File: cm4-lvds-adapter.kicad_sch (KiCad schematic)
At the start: 19 parts, among them J1 Plug_Molex_SlimStack_2x15_538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, J2 JST_SM_1x10_SM10B-SURS-TF-LF-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

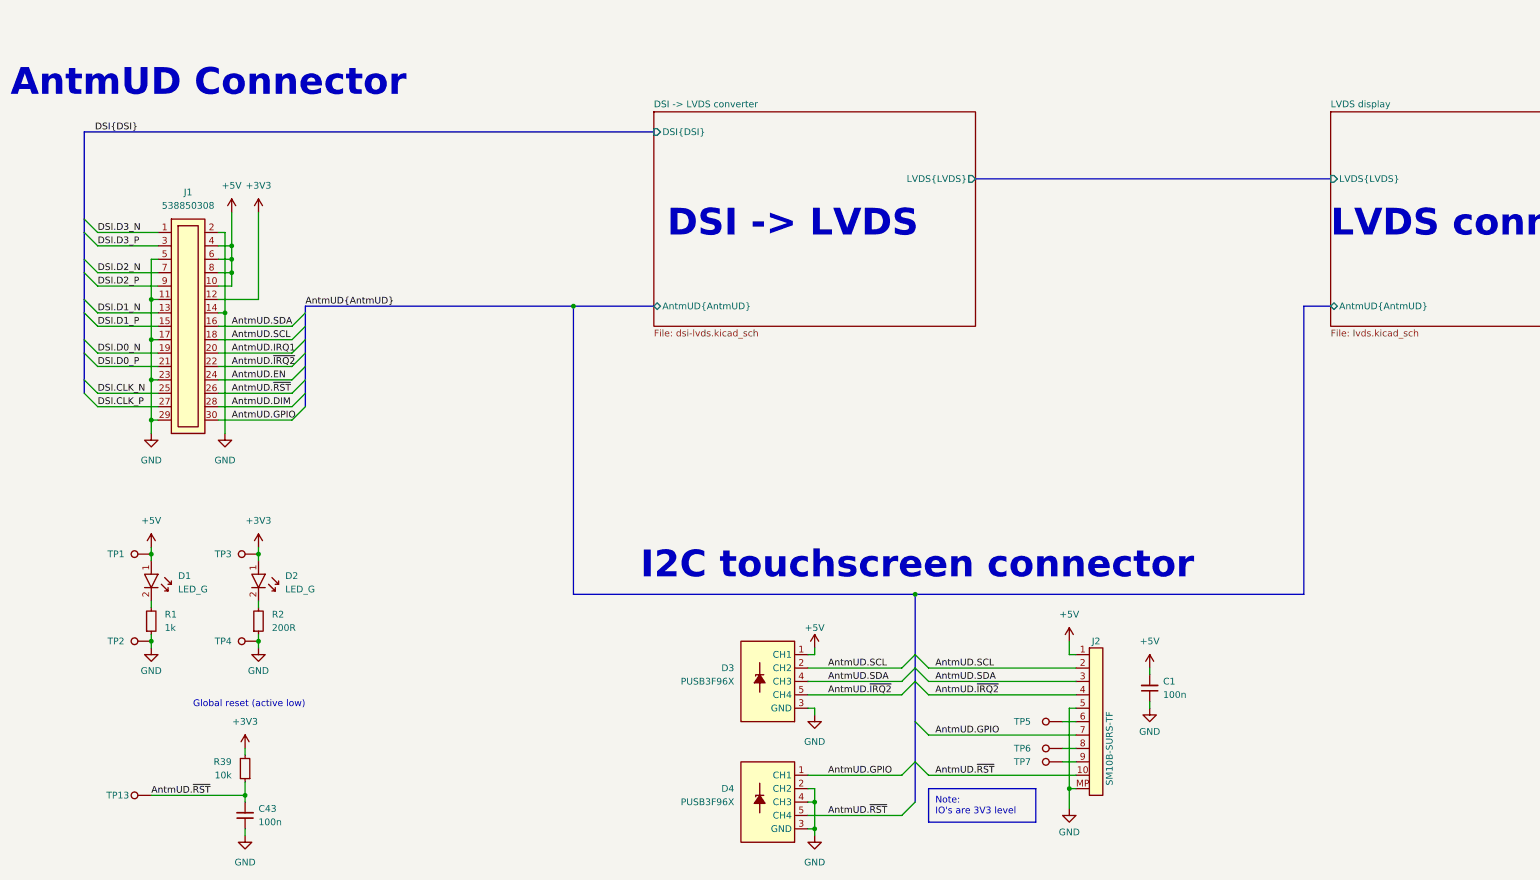
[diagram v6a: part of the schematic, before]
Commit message: [#54932] Sch: update net labels
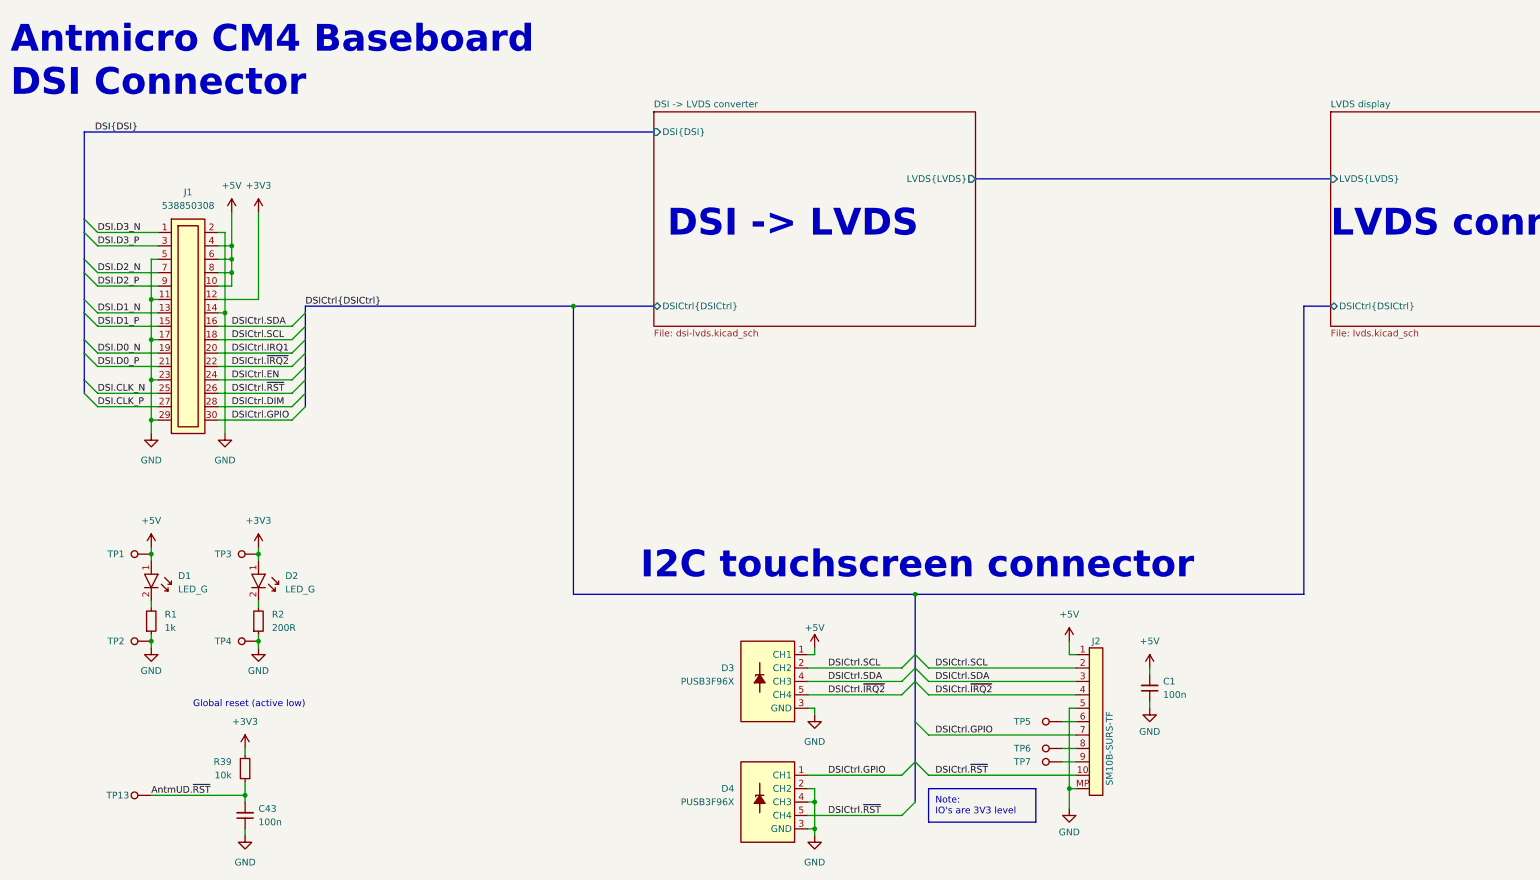
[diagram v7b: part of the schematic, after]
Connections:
- net AntmUD.~{RST}: no longer D4.5 (CH4), D4.6 (CH4), J1.26, J2.10
- net AntmUD.DIM renamed DSICtrl.DIM
- net AntmUD.EN renamed DSICtrl.EN
- net AntmUD.GPIO renamed DSICtrl.GPIO
- net AntmUD.IRQ1 renamed DSICtrl.IRQ1
- net AntmUD.SCL renamed DSICtrl.SCL
- net AntmUD.SDA renamed DSICtrl.SDA
- net AntmUD.~{IRQ2} renamed DSICtrl.~{IRQ2}
- new net DSICtrl.~{RST}: D4.5 (CH4), D4.6 (CH4), J1.26, J2.10
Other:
- sheet DSI -> LVDS converter ports: added DSICtrl{DSICtrl}; removed AntmUD{AntmUD}
- sheet LVDS display ports: added DSICtrl{DSICtrl}; removed AntmUD{AntmUD}
- note added: "Antmicro CM4 Baseboard DSI Connector"
- note removed: "AntmUD Connector"
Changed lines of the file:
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@@
     (effects (font (size 1.27 1.27)) (justify right bottom))
   )
-  (text "AntmUD Connector" (at 60.96 85.09 0)
+  (text "Antmicro CM4 Baseboard \nDSI Connector" (at 60.96 85.09 0)
     (effects (font (size 5.08 5.08) (thickness 1.016) bold) (justify left bottom))
   )
@@
     (effects (font (size 1.27 1.27)) (justify left bottom))
   )
-  (label "AntmUD.~{IRQ2}" (at 215.9 198.12 0) (fields_autoplaced)
-    (effects (font (size 1.27 1.27)) (justify left bottom))
-  )
-  (label "AntmUD.SCL" (at 215.9 193.04 0) (fields_autoplaced)
-    (effects (font (size 1.27 1.27)) (justify left bottom))
-  )
-  (label "AntmUD.SDA" (at 102.87 128.27 0) (fields_autoplaced)
-    (effects (font (size 1.27 1.27)) (justify left bottom))
-  )
-  (label "AntmUD.SDA" (at 215.9 195.58 0) (fields_autoplaced)
+  (label "DSICtrl.~{IRQ2}" (at 215.9 198.12 0) (fields_autoplaced)
+    (effects (font (size 1.27 1.27)) (justify left bottom))
+  )
+  (label "DSICtrl.SCL" (at 215.9 193.04 0) (fields_autoplaced)
+    (effects (font (size 1.27 1.27)) (justify left bottom))
+  )
+  (label "DSICtrl.SDA" (at 102.87 128.27 0) (fields_autoplaced)
+    (effects (font (size 1.27 1.27)) (justify left bottom))
+  )
+  (label "DSICtrl.SDA" (at 215.9 195.58 0) (fields_autoplaced)
     (effects (font (size 1.27 1.27)) (justify left bottom))
   )
@@
     (effects (font (size 1.27 1.27)) (justify right bottom))
   )
-  (label "AntmUD.SCL" (at 236.22 193.04 0) (fields_autoplaced)
-    (effects (font (size 1.27 1.27)) (justify left bottom))
-  )
-  (label "AntmUD.~{RST}" (at 215.9 220.98 0) (fields_autoplaced)
-    (effects (font (size 1.27 1.27)) (justify left bottom))
-  )
-  (label "AntmUD.SDA" (at 236.22 195.58 0) (fields_autoplaced)
-    (effects (font (size 1.27 1.27)) (justify left bottom))
-  )
-  (label "AntmUD.EN" (at 102.87 138.43 0) (fields_autoplaced)
-    (effects (font (size 1.27 1.27)) (justify left bottom))
-  )
-  (label "AntmUD{AntmUD}" (at 116.84 124.46 0) (fields_autoplaced)
-    (effects (font (size 1.27 1.27)) (justify left bottom))
-  )
-  (label "AntmUD.~{IRQ2}" (at 102.87 135.89 0) (fields_autoplaced)
-    (effects (font (size 1.27 1.27)) (justify left bottom))
-  )
-  (label "AntmUD.SCL" (at 102.87 130.81 0) (fields_autoplaced)
+  (label "DSICtrl.SCL" (at 236.22 193.04 0) (fields_autoplaced)
+    (effects (font (size 1.27 1.27)) (justify left bottom))
+  )
+  (label "DSICtrl.~{RST}" (at 215.9 220.98 0) (fields_autoplaced)
+    (effects (font (size 1.27 1.27)) (justify left bottom))
+  )
+  (label "DSICtrl.SDA" (at 236.22 195.58 0) (fields_autoplaced)
+    (effects (font (size 1.27 1.27)) (justify left bottom))
+  )
+  (label "DSICtrl.EN" (at 102.87 138.43 0) (fields_autoplaced)
+    (effects (font (size 1.27 1.27)) (justify left bottom))
+  )
+  (label "DSICtrl{DSICtrl}" (at 116.84 124.46 0) (fields_autoplaced)
+    (effects (font (size 1.27 1.27)) (justify left bottom))
+  )
+  (label "DSICtrl.~{IRQ2}" (at 102.87 135.89 0) (fields_autoplaced)
+    (effects (font (size 1.27 1.27)) (justify left bottom))
+  )
+  (label "DSICtrl.SCL" (at 102.87 130.81 0) (fields_autoplaced)
     (effects (font (size 1.27 1.27)) (justify left bottom))
   )
@@
     (effects (font (size 1.27 1.27)) (justify left bottom))
   )
-  (label "AntmUD.~{RST}" (at 236.22 213.36 0) (fields_autoplaced)
-    (effects (font (size 1.27 1.27)) (justify left bottom))
-  )
-  (label "AntmUD.DIM" (at 102.87 143.51 0) (fields_autoplaced)
-    (effects (font (size 1.27 1.27)) (justify left bottom))
-  )
-  (label "AntmUD.GPIO" (at 236.22 205.74 0) (fields_autoplaced)
+  (label "DSICtrl.~{RST}" (at 236.22 213.36 0) (fields_autoplaced)
+    (effects (font (size 1.27 1.27)) (justify left bottom))
+  )
+  (label "DSICtrl.DIM" (at 102.87 143.51 0) (fields_autoplaced)
+    (effects (font (size 1.27 1.27)) (justify left bottom))
+  )
+  (label "DSICtrl.GPIO" (at 236.22 205.74 0) (fields_autoplaced)
     (effects (font (size 1.27 1.27)) (justify left bottom))
   )
@@
     (effects (font (size 1.27 1.27)) (justify left bottom))
   )
-  (label "AntmUD.~{IRQ2}" (at 236.22 198.12 0) (fields_autoplaced)
+  (label "DSICtrl.~{IRQ2}" (at 236.22 198.12 0) (fields_autoplaced)
     (effects (font (size 1.27 1.27)) (justify left bottom))
   )
@@
     (effects (font (size 1.27 1.27)) (justify left bottom))
   )
-  (label "AntmUD.GPIO" (at 215.9 213.36 0) (fields_autoplaced)
+  (label "DSICtrl.GPIO" (at 215.9 213.36 0) (fields_autoplaced)
     (effects (font (size 1.27 1.27)) (justify left bottom))
   )
@@
     (effects (font (size 1.27 1.27)) (justify left bottom))
   )
-  (label "AntmUD.~{RST}" (at 102.87 140.97 0) (fields_autoplaced)
-    (effects (font (size 1.27 1.27)) (justify left bottom))
-  )
-  (label "AntmUD.GPIO" (at 102.87 146.05 0) (fields_autoplaced)
-    (effects (font (size 1.27 1.27)) (justify left bottom))
-  )
-  (label "AntmUD.IRQ1" (at 102.87 133.35 0) (fields_autoplaced)
+  (label "DSICtrl.~{RST}" (at 102.87 140.97 0) (fields_autoplaced)
+    (effects (font (size 1.27 1.27)) (justify left bottom))
+  )
+  (label "DSICtrl.GPIO" (at 102.87 146.05 0) (fields_autoplaced)
+    (effects (font (size 1.27 1.27)) (justify left bottom))
+  )
+  (label "DSICtrl.IRQ1" (at 102.87 133.35 0) (fields_autoplaced)
     (effects (font (size 1.27 1.27)) (justify left bottom))
   )
@@
       (effects (font (size 1.27 1.27)) (justify left))
     )
-    (pin "AntmUD{AntmUD}" bidirectional (at 311.15 124.46 180)
+    (pin "DSICtrl{DSICtrl}" bidirectional (at 311.15 124.46 180)
       (effects (font (size 1.27 1.27)) (justify left))
     )
@@
       (effects (font (size 1.27 1.27)) (justify right))
     )
-    (pin "AntmUD{AntmUD}" bidirectional (at 182.88 124.46 180)
+    (pin "DSICtrl{DSICtrl}" bidirectional (at 182.88 124.46 180)
       (effects (font (size 1.27 1.27)) (justify left))
     )

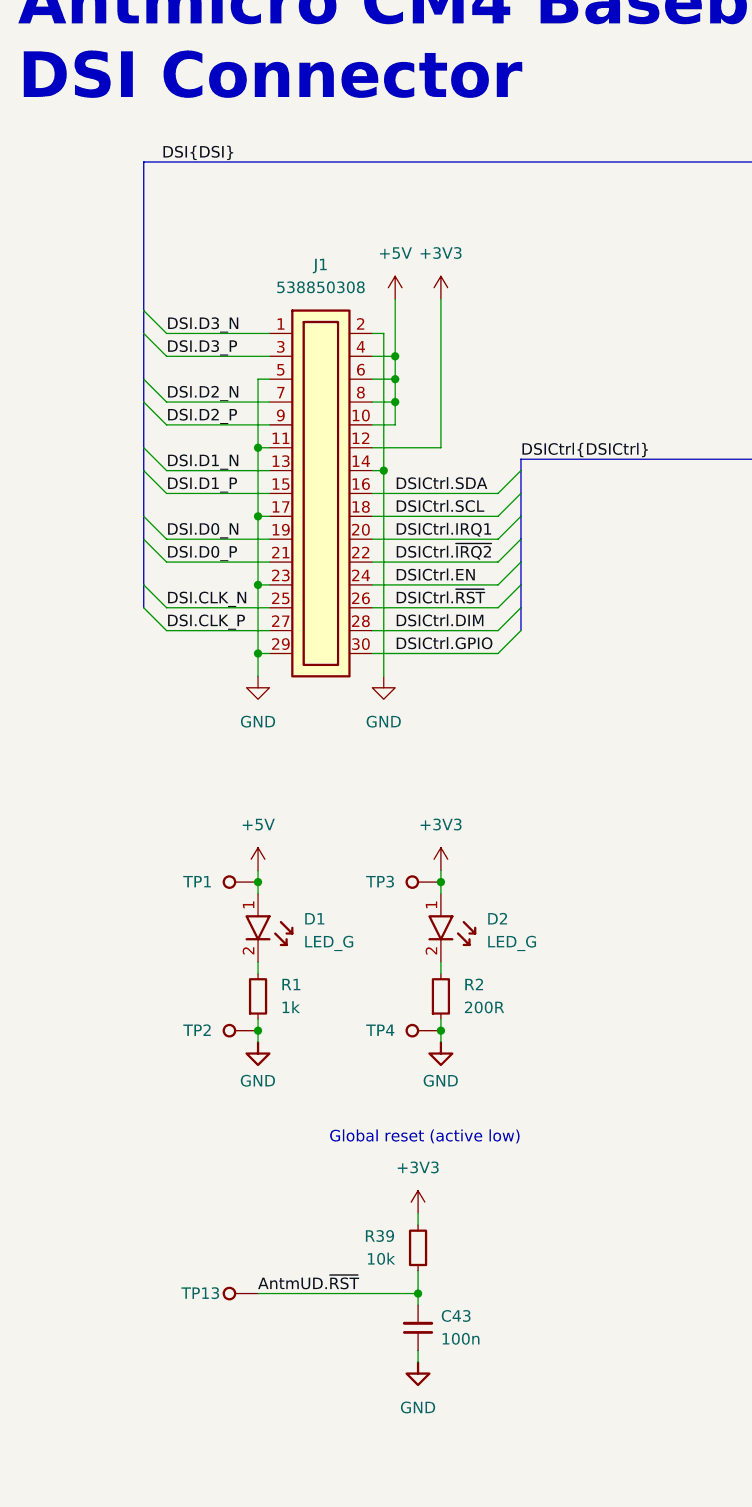
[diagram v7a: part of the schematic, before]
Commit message: [#54932] Change adapter connector (from 2x15 to 2x20)
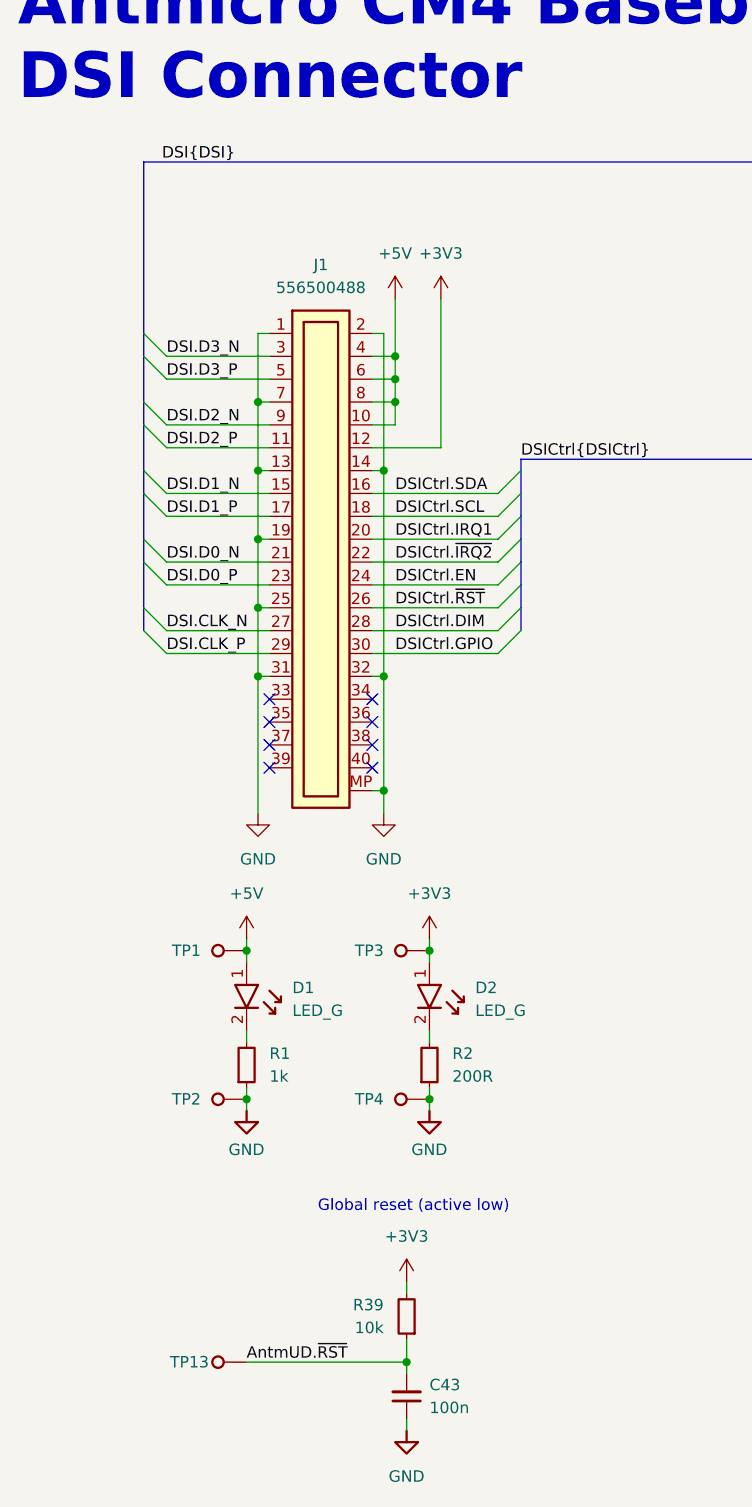
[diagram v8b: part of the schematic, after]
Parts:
- J1: footprint antmicro-footprints:Conn_Plug_Molex_SlimStack_2x15_538850308 -> antmicro-footprints:Conn_Plug_Molex_SlimStack_2x20_556500488; symbol antmicroB2BConnectors:Plug_Molex_SlimStack_2x15_538850308 -> antmicroB2BConnectors:Plug_Molex_SlimStack_2x20_556500488; MPN 538850308 -> 556500488
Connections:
- net DSI.CLK_N: now also J1.27; no longer J1.25
- net DSI.CLK_P: now also J1.29; no longer J1.27
- net DSI.D0_N: now also J1.21; no longer J1.19
- net DSI.D0_P: now also J1.23; no longer J1.21
- net DSI.D1_N: now also J1.15; no longer J1.13
- net DSI.D1_P: now also J1.17; no longer J1.15
- net DSI.D2_N: now also J1.9; no longer J1.7
- net DSI.D2_P: now also J1.11; no longer J1.9
- net DSI.D3_N: now also J1.3; no longer J1.1
- net DSI.D3_P: now also J1.5; no longer J1.3
- net GND: now also J1.1, J1.13, J1.19, J1.25, J1.31, J1.32, J1.7, J1.MP; no longer J1.11, J1.17, J1.23, J1.29, J1.5
- no-connect marks 0 -> 8
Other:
- moved on the sheet: C43, D1, D2, R1, R2, R39, TP1, TP13, TP2, TP3, TP4
